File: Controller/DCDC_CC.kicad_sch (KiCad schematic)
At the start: 8 parts, among them U7 BP1808

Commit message: pcb stuff
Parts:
- D6: footprint Diode_SMD:D_SMA -> Diode_SMD:D_SOD-123F
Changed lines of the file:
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@@
       (effects (font (size 1.27 1.27)) (justify left))
     )
-    (property "Footprint" "Diode_SMD:D_SMA" (id 2) (at 158.75 99.06 0)
+    (property "Footprint" "Diode_SMD:D_SOD-123F" (id 2) (at 158.75 99.06 0)
       (effects (font (size 1.27 1.27)) hide)
     )

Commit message: finish PCB
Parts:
- renumbered C16 to C12, C17 to C13, C18 to C14, C19 to C15, D6 to D5, L3 to L2, R5 to R3, U7 to U6
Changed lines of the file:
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@@
   (symbol (lib_id "Device:L") (at 170.18 111.76 90)
     (in_bom yes) (on_board yes)
-    (property "Reference" "L3" (id 0) (at 168.91 114.3 90))
+    (property "Reference" "L2" (id 0) (at 168.91 114.3 90))
     (property "Value" "10u" (id 1) (at 172.72 114.3 90))
     (property "Footprint" "LeoDJ-kicad:L_0520" (id 2) (at 170.18 111.76 0)
@@
   (symbol (lib_id "Device:R") (at 182.88 95.25 90)
     (in_bom yes) (on_board yes) (fields_autoplaced)
-    (property "Reference" "R5" (id 0) (at 182.88 88.9 90))
+    (property "Reference" "R3" (id 0) (at 182.88 88.9 90))
     (property "Value" "R" (id 1) (at 182.88 91.44 90))
     (property "Footprint" "Resistor_SMD:R_1206_3216Metric" (id 2) (at 182.88 97.028 90)
@@
   (symbol (lib_id "Device:D_Schottky") (at 158.75 99.06 270)
     (in_bom yes) (on_board yes)
-    (property "Reference" "D6" (id 0) (at 161.29 97.7899 90)
+    (property "Reference" "D5" (id 0) (at 161.29 97.7899 90)
       (effects (font (size 1.27 1.27)) (justify left))
     )
@@
   (symbol (lib_id "Device:C") (at 105.41 104.14 0)
     (in_bom yes) (on_board yes)
-    (property "Reference" "C16" (id 0) (at 100.33 102.8699 0)
+    (property "Reference" "C12" (id 0) (at 100.33 102.8699 0)
       (effects (font (size 1.27 1.27)) (justify left))
     )
@@
   (symbol (lib_id "Device:C") (at 149.86 101.6 0)
     (in_bom yes) (on_board yes)
-    (property "Reference" "C17" (id 0) (at 151.13 99.0599 0)
+    (property "Reference" "C13" (id 0) (at 151.13 99.0599 0)
       (effects (font (size 1.27 1.27)) (justify left))
     )
@@
   (symbol (lib_id "Device:C_Polarized") (at 167.64 101.6 0)
     (in_bom yes) (on_board yes) (fields_autoplaced)
-    (property "Reference" "C18" (id 0) (at 171.45 100.3299 0)
+    (property "Reference" "C14" (id 0) (at 171.45 100.3299 0)
       (effects (font (size 1.27 1.27)) (justify left))
     )
@@
   (symbol (lib_id "Device:C") (at 179.07 101.6 180)
     (in_bom yes) (on_board yes)
-    (property "Reference" "C19" (id 0) (at 182.88 101.6 0))
+    (property "Reference" "C15" (id 0) (at 182.88 101.6 0))
     (property "Value" "1u" (id 1) (at 182.88 104.14 0))
     (property "Footprint" "Capacitor_SMD:C_0603_1608Metric" (id 2) (at 178.1048 97.79 0)
@@
   (symbol (lib_id "LeoDJ:BP1808") (at 135.89 96.52 0)
     (in_bom yes) (on_board yes) (fields_autoplaced)
-    (property "Reference" "U7" (id 0) (at 135.255 86.36 0))
+    (property "Reference" "U6" (id 0) (at 135.255 86.36 0))
     (property "Value" "BP1808" (id 1) (at 135.255 88.9 0))
     (property "Footprint" "Package_SO:SOIC-8-1EP_3.9x4.9mm_P1.27mm_EP2.41x3.3mm" (id 2) (at 142.24 93.98 0)

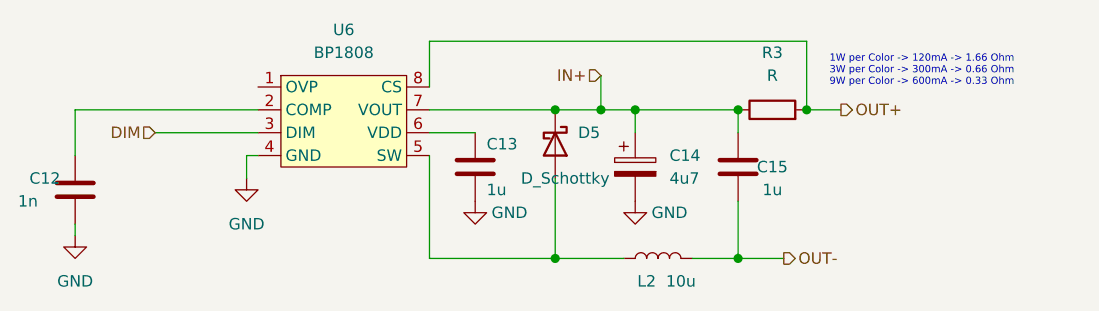
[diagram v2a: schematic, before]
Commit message: switch to different LDO
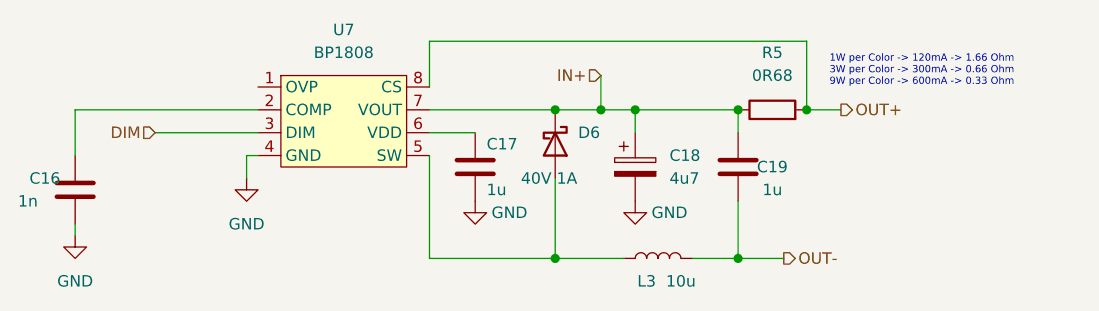
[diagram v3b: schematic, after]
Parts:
- D6: renamed from D5; value D_Schottky -> 40V 1A; footprint Diode_SMD:D_SOD-123F -> Diode_SMD:D_SOD-123; LCSC (none) -> C8598
- R5: renamed from R3; value R -> 0R68
- U7: renamed from U6; LCSC (none) -> C85659
- renumbered C12 to C16, C13 to C17, C14 to C18, C15 to C19, L2 to L3
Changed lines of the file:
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@@
   (symbol (lib_id "Device:L") (at 170.18 111.76 90)
     (in_bom yes) (on_board yes)
-    (property "Reference" "L2" (id 0) (at 168.91 114.3 90))
+    (property "Reference" "L3" (id 0) (at 168.91 114.3 90))
     (property "Value" "10u" (id 1) (at 172.72 114.3 90))
     (property "Footprint" "LeoDJ-kicad:L_0520" (id 2) (at 170.18 111.76 0)
@@
   (symbol (lib_id "Device:R") (at 182.88 95.25 90)
     (in_bom yes) (on_board yes) (fields_autoplaced)
-    (property "Reference" "R3" (id 0) (at 182.88 88.9 90))
-    (property "Value" "R" (id 1) (at 182.88 91.44 90))
+    (property "Reference" "R5" (id 0) (at 182.88 88.9 90))
+    (property "Value" "0R68" (id 1) (at 182.88 91.44 90))
     (property "Footprint" "Resistor_SMD:R_1206_3216Metric" (id 2) (at 182.88 97.028 90)
       (effects (font (size 1.27 1.27)) hide)
@@
   (symbol (lib_id "Device:D_Schottky") (at 158.75 99.06 270)
     (in_bom yes) (on_board yes)
-    (property "Reference" "D5" (id 0) (at 161.29 97.7899 90)
+    (property "Reference" "D6" (id 0) (at 161.29 97.7899 90)
       (effects (font (size 1.27 1.27)) (justify left))
     )
-    (property "Value" "D_Schottky" (id 1) (at 154.94 102.8699 90)
+    (property "Value" "40V 1A" (id 1) (at 154.94 102.8699 90)
       (effects (font (size 1.27 1.27)) (justify left))
     )
-    (property "Footprint" "Diode_SMD:D_SOD-123F" (id 2) (at 158.75 99.06 0)
+    (property "Footprint" "Diode_SMD:D_SOD-123" (id 2) (at 158.75 99.06 0)
       (effects (font (size 1.27 1.27)) hide)
     )
     (property "Datasheet" "~" (id 3) (at 158.75 99.06 0)
+      (effects (font (size 1.27 1.27)) hide)
+    )
+    (property "LCSC" "C8598" (id 4) (at 158.75 99.06 90)
       (effects (font (size 1.27 1.27)) hide)
     )
@@
   (symbol (lib_id "Device:C") (at 105.41 104.14 0)
     (in_bom yes) (on_board yes)
-    (property "Reference" "C12" (id 0) (at 100.33 102.8699 0)
+    (property "Reference" "C16" (id 0) (at 100.33 102.8699 0)
       (effects (font (size 1.27 1.27)) (justify left))
     )
@@
   (symbol (lib_id "Device:C") (at 149.86 101.6 0)
     (in_bom yes) (on_board yes)
-    (property "Reference" "C13" (id 0) (at 151.13 99.0599 0)
+    (property "Reference" "C17" (id 0) (at 151.13 99.0599 0)
       (effects (font (size 1.27 1.27)) (justify left))
     )
@@
   (symbol (lib_id "Device:C_Polarized") (at 167.64 101.6 0)
     (in_bom yes) (on_board yes) (fields_autoplaced)
-    (property "Reference" "C14" (id 0) (at 171.45 100.3299 0)
+    (property "Reference" "C18" (id 0) (at 171.45 100.3299 0)
       (effects (font (size 1.27 1.27)) (justify left))
     )
@@
   (symbol (lib_id "Device:C") (at 179.07 101.6 180)
     (in_bom yes) (on_board yes)
-    (property "Reference" "C15" (id 0) (at 182.88 101.6 0))
+    (property "Reference" "C19" (id 0) (at 182.88 101.6 0))
     (property "Value" "1u" (id 1) (at 182.88 104.14 0))
     (property "Footprint" "Capacitor_SMD:C_0603_1608Metric" (id 2) (at 178.1048 97.79 0)
@@
   (symbol (lib_id "LeoDJ:BP1808") (at 135.89 96.52 0)
     (in_bom yes) (on_board yes) (fields_autoplaced)
-    (property "Reference" "U6" (id 0) (at 135.255 86.36 0))
+    (property "Reference" "U7" (id 0) (at 135.255 86.36 0))
     (property "Value" "BP1808" (id 1) (at 135.255 88.9 0))
     (property "Footprint" "Package_SO:SOIC-8-1EP_3.9x4.9mm_P1.27mm_EP2.41x3.3mm" (id 2) (at 142.24 93.98 0)
@@
       (effects (font (size 1.27 1.27)) hide)
     )
+    (property "LCSC" "C85659" (id 4) (at 135.89 96.52 0)
+      (effects (font (size 1.27 1.27)) hide)
+    )

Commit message: generate fabrication files
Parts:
- D5: renamed from D6; value 40V 1A -> 40V 1A Schottky
- renumbered C16 to C12, C17 to C13, C18 to C14, C19 to C15, L3 to L2, R5 to R3, U7 to U6
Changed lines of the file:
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@@
   (symbol (lib_id "power:GND") (at 105.41 109.22 0)
     (in_bom yes) (on_board yes) (fields_autoplaced)
-    (property "Reference" "#PWR0132" (id 0) (at 105.41 115.57 0)
+    (property "Reference" "#PWR0128" (id 0) (at 105.41 115.57 0)
       (effects (font (size 1.27 1.27)) hide)
     )
@@
   (symbol (lib_id "power:GND") (at 124.46 102.87 0)
     (in_bom yes) (on_board yes) (fields_autoplaced)
-    (property "Reference" "#PWR0133" (id 0) (at 124.46 109.22 0)
+    (property "Reference" "#PWR0129" (id 0) (at 124.46 109.22 0)
       (effects (font (size 1.27 1.27)) hide)
     )
@@
   (symbol (lib_id "power:GND") (at 149.86 105.41 0)
     (in_bom yes) (on_board yes)
-    (property "Reference" "#PWR0130" (id 0) (at 149.86 111.76 0)
+    (property "Reference" "#PWR0126" (id 0) (at 149.86 111.76 0)
       (effects (font (size 1.27 1.27)) hide)
     )
@@
   (symbol (lib_id "power:GND") (at 167.64 105.41 0)
     (in_bom yes) (on_board yes)
-    (property "Reference" "#PWR0131" (id 0) (at 167.64 111.76 0)
+    (property "Reference" "#PWR0127" (id 0) (at 167.64 111.76 0)
       (effects (font (size 1.27 1.27)) hide)
     )
@@
   (symbol (lib_id "Device:L") (at 170.18 111.76 90)
     (in_bom yes) (on_board yes)
-    (property "Reference" "L3" (id 0) (at 168.91 114.3 90))
+    (property "Reference" "L2" (id 0) (at 168.91 114.3 90))
     (property "Value" "10u" (id 1) (at 172.72 114.3 90))
     (property "Footprint" "LeoDJ-kicad:L_0520" (id 2) (at 170.18 111.76 0)
@@
   (symbol (lib_id "Device:R") (at 182.88 95.25 90)
     (in_bom yes) (on_board yes) (fields_autoplaced)
-    (property "Reference" "R5" (id 0) (at 182.88 88.9 90))
+    (property "Reference" "R3" (id 0) (at 182.88 88.9 90))
     (property "Value" "0R68" (id 1) (at 182.88 91.44 90))
     (property "Footprint" "Resistor_SMD:R_1206_3216Metric" (id 2) (at 182.88 97.028 90)
@@
   (symbol (lib_id "Device:D_Schottky") (at 158.75 99.06 270)
     (in_bom yes) (on_board yes)
-    (property "Reference" "D6" (id 0) (at 161.29 97.7899 90)
+    (property "Reference" "D5" (id 0) (at 161.29 97.7899 90)
       (effects (font (size 1.27 1.27)) (justify left))
     )
-    (property "Value" "40V 1A" (id 1) (at 154.94 102.8699 90)
+    (property "Value" "40V 1A Schottky" (id 1) (at 154.178 104.1399 90)
       (effects (font (size 1.27 1.27)) (justify left))
     )
@@
   (symbol (lib_id "Device:C") (at 105.41 104.14 0)
     (in_bom yes) (on_board yes)
-    (property "Reference" "C16" (id 0) (at 100.33 102.8699 0)
+    (property "Reference" "C12" (id 0) (at 100.33 102.8699 0)
       (effects (font (size 1.27 1.27)) (justify left))
     )
@@
   (symbol (lib_id "Device:C") (at 149.86 101.6 0)
     (in_bom yes) (on_board yes)
-    (property "Reference" "C17" (id 0) (at 151.13 99.0599 0)
+    (property "Reference" "C13" (id 0) (at 151.13 99.0599 0)
       (effects (font (size 1.27 1.27)) (justify left))
     )
@@
   (symbol (lib_id "Device:C_Polarized") (at 167.64 101.6 0)
     (in_bom yes) (on_board yes) (fields_autoplaced)
-    (property "Reference" "C18" (id 0) (at 171.45 100.3299 0)
+    (property "Reference" "C14" (id 0) (at 171.45 100.3299 0)
       (effects (font (size 1.27 1.27)) (justify left))
     )
@@
   (symbol (lib_id "Device:C") (at 179.07 101.6 180)
     (in_bom yes) (on_board yes)
-    (property "Reference" "C19" (id 0) (at 182.88 101.6 0))
+    (property "Reference" "C15" (id 0) (at 182.88 101.6 0))
     (property "Value" "1u" (id 1) (at 182.88 104.14 0))
     (property "Footprint" "Capacitor_SMD:C_0603_1608Metric" (id 2) (at 178.1048 97.79 0)
@@
   (symbol (lib_id "LeoDJ:BP1808") (at 135.89 96.52 0)
     (in_bom yes) (on_board yes) (fields_autoplaced)
-    (property "Reference" "U7" (id 0) (at 135.255 86.36 0))
+    (property "Reference" "U6" (id 0) (at 135.255 86.36 0))
     (property "Value" "BP1808" (id 1) (at 135.255 88.9 0))
     (property "Footprint" "Package_SO:SOIC-8-1EP_3.9x4.9mm_P1.27mm_EP2.41x3.3mm" (id 2) (at 142.24 93.98 0)
